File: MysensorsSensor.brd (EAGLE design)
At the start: 26.2 x 44.1 mm, 41 parts, among them IC1 TS5205, IC2 AT25DF512C-SSHN-B, IC3 ATSHA204A, Q1 FC-12M, U1 ATMEGA328P-AU

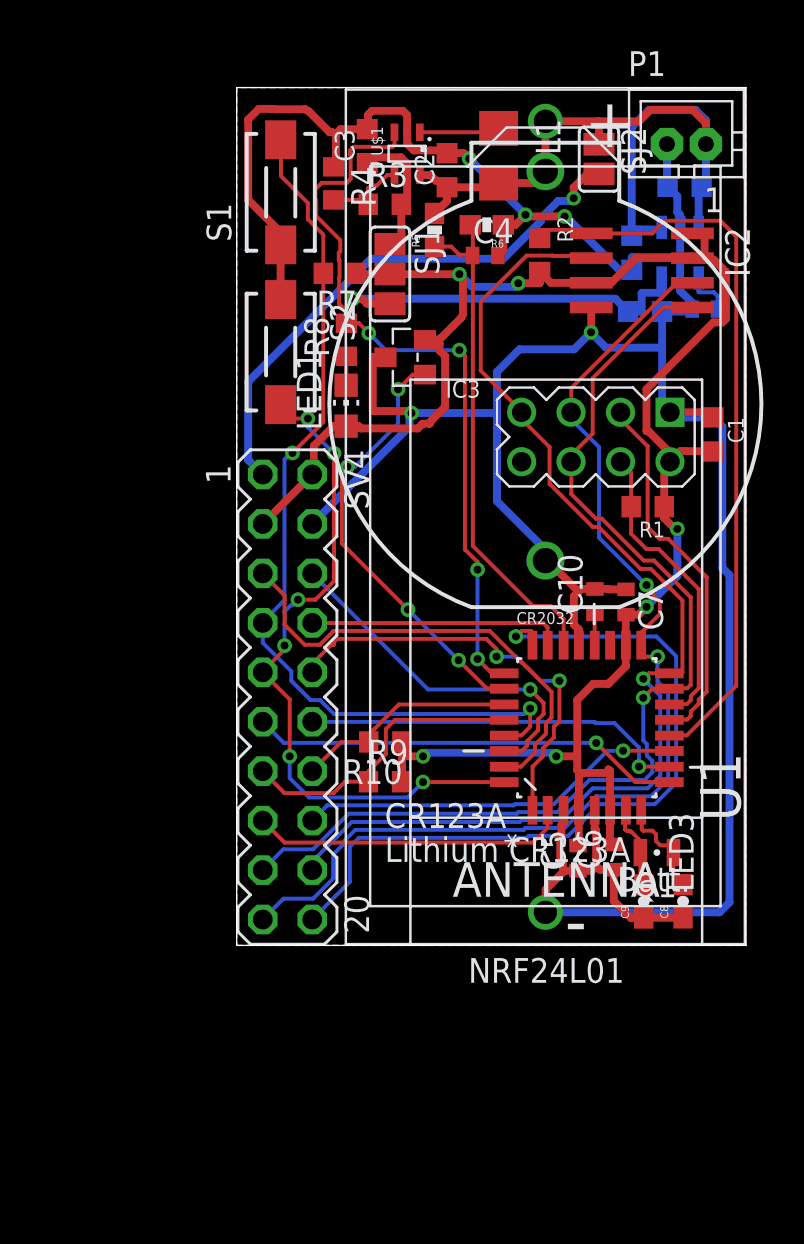
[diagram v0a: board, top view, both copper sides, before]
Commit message: 1. fix wrong boost converter footprint 2. connect led to A1 pin instead of A2 (which was used by the boost converter enable 3. change crystal footrint but not change the pcb
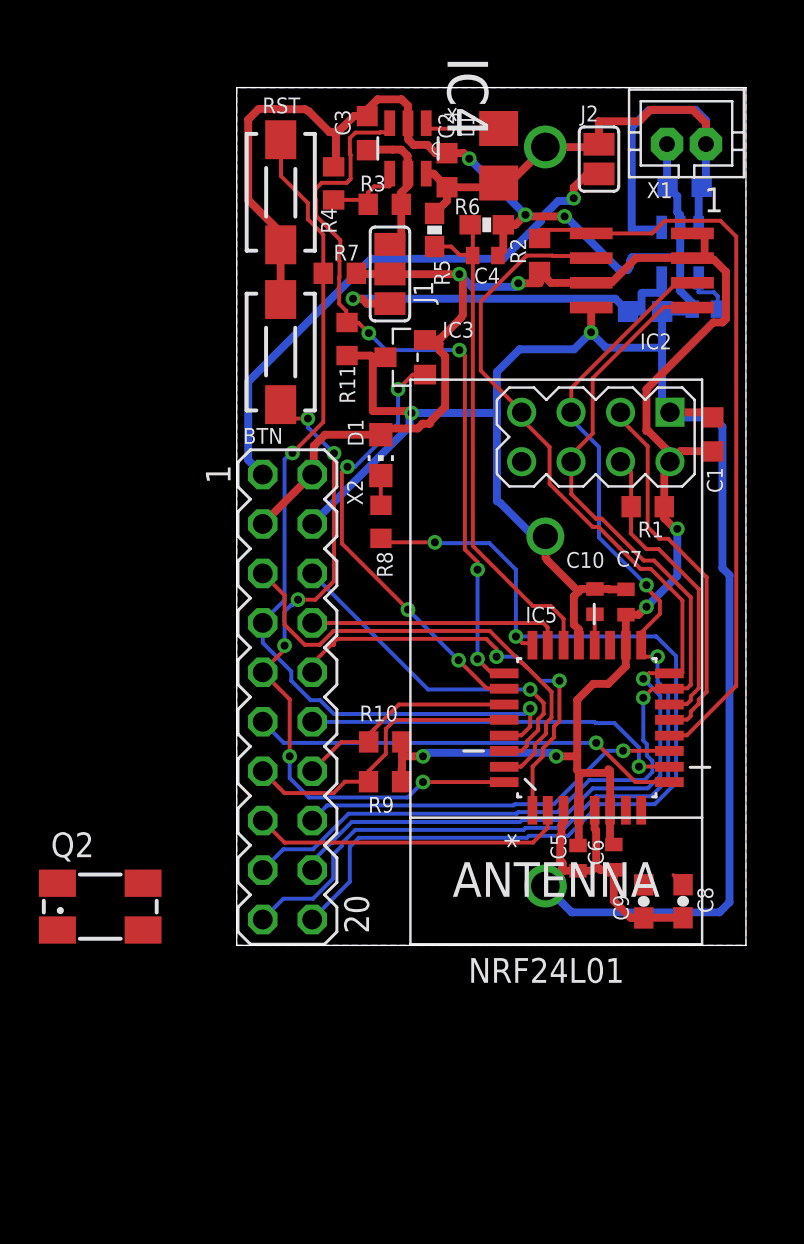
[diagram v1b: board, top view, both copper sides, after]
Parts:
- removed C11: 10u, rcl:C0603K
- removed LED1: (no value), led:CHIP-LED0805
- removed Q1: FC-12M, crystal:FC-12M
- removed U$1: MCP1640, pulseoxparts:SOT23-6
- added D1: (no value), led:CHIP-LED0805
- added IC4: MCP1640CT-I/CHY, Microchip_By_element14_Batch_1:SOT95P270X145-6N
- added Q2: (no value), crystal:CTS406
- added R11: 1M, resistor:R0603
- C10, C4, C5, C6, C7: value (none) -> 100n
- C12: value (none) -> 10n
- C8, C9: value 10u -> 22p
- CR123A: value (none) -> BAT_PACKCR123A; device Battery:TAKACHI_CR123A -> batteries:BH123A
- CR2032: value (none) -> 3V
- L1: value (none) -> 4.7u
- R1, R2, R3, R5, R7: value 100k -> 1M
- R10, R9: value 100k -> 10k
- R4: value 100k -> 620k
- R8: value 100k -> 1k
- moved R8 9.52 mm to (7.41, 21.8), turned to 270 degrees
- moved CR2032 1.24 mm to (15.9, 29.2), flipped to the bottom
- moved C3 0.67 mm to (6.71, 41.7)
- flipped CR123A to the bottom, turned to 90 degrees
- renumbered P1 to X1, S1 to RST, S2 to BTN, SJ1 to J1, SJ2 to J2, SV4 to X2, U1 to IC5
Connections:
- net A1: now also R8.2
- net A2: now also IC4.3, R11.1; no longer R8.2, U$1.P$3
- net GND: now also IC4.2, R11.2; no longer C11.2, U$1.P$2
- net N$1: now also IC4.4; no longer U$1.P$4
- net N$10: now also D1.C; no longer LED1.C
- net N$2: now also Q2.1; no longer Q1.1
- net N$4: now also IC4.1; no longer U$1.P$1
- net N$6: now also Q2.3; no longer Q1.2
- net VBAT: now also IC4.6; no longer C11.1, U$1.P$6
- net VBOOST: now also IC4.5; no longer U$1.P$5
- net VCC: now also D1.A; no longer LED1.A
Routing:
- net A1: track 39.9 -> 50.4 mm, vias 1 -> 2
- net N$2: track 5.31 -> 0.70 mm
- net N$6: track 4.37 -> 0.00 mm
- net VBAT: track 39.5 -> 36.9 mm
- net GND: track 163.2 -> 164.4 mm
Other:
- board text added: "MySensors 1.0"
- board text removed: "LED3"

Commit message: 1. rearrange nfr24l01 connector and atmega328p chip
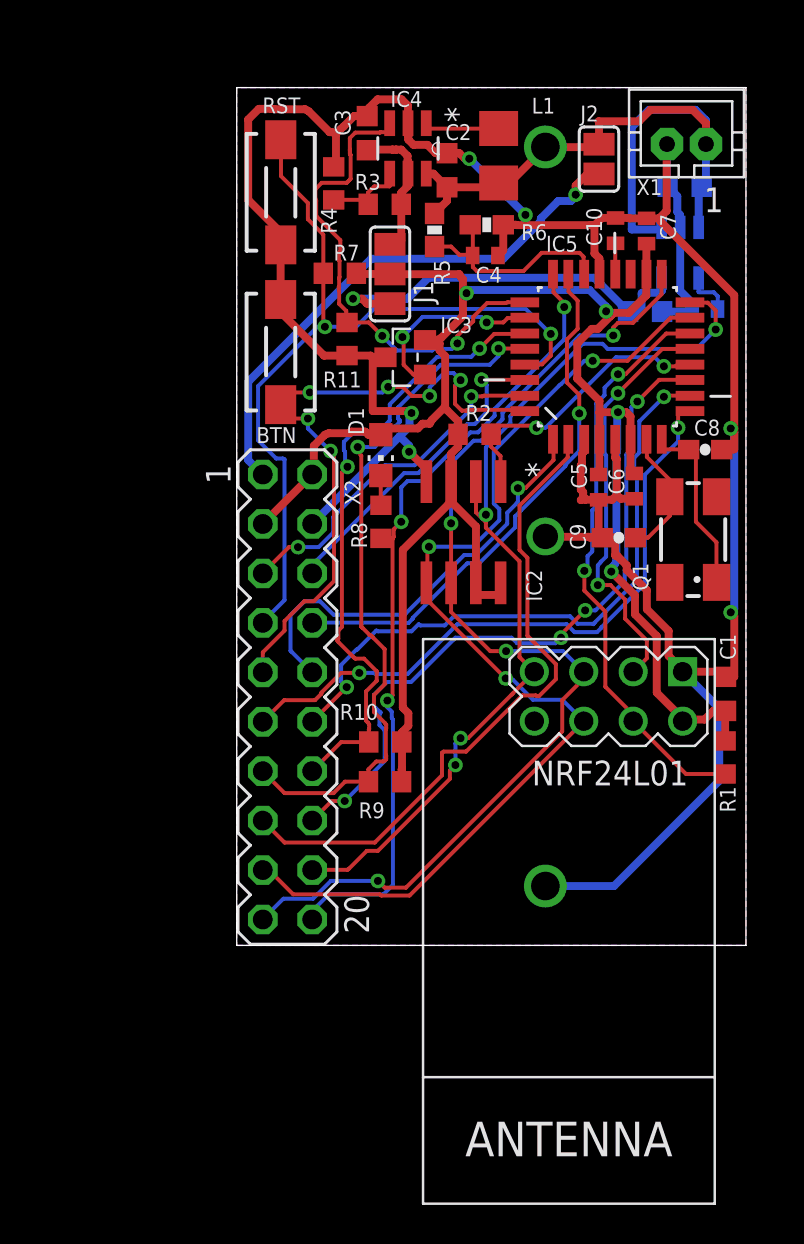
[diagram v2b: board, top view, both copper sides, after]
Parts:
- removed Q2: (no value), crystal:CTS406
- added Q1: (no value), crystal:CTS406
- moved C8 23.2 mm to (24.1, 25.5), turned to 180 degrees
- moved C10 19.1 mm to (19.5, 36.7)
- moved C5 19.1 mm to (18.6, 23.5)
- moved C7 19.1 mm to (21.1, 36.7)
- moved IC5 19.1 mm to (19.0, 30.2)
- moved C6 19.1 mm to (20.4, 23.6)
- moved C9 18.7 mm to (19.6, 20.9), turned to 0 degrees
- moved IC2 16.3 mm to (11.7, 21.2), turned to 180 degrees
- moved R1 13.5 mm to (25.1, 9.66), turned to 270 degrees
- moved C1 13.3 mm to (25.1, 12.9)
- moved NRF24L01 13.3 mm to (16.6, 1.36)
- moved R2 9.80 mm to (12.2, 26.3), turned to 180 degrees
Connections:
- net N$2: now also Q1.1; no longer Q2.1
- net N$6: now also Q1.3; no longer Q2.3
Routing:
- net D8: track 38.8 -> 15.1 mm, vias 0 -> 2
- net A4: track 11.5 -> 32.8 mm, vias 0 -> 2
- net A5: track 15.5 -> 36.6 mm, vias 0 -> 2
- net D4: track 16.3 -> 33.8 mm
- net D7: track 19.8 -> 37.0 mm, vias 1 -> 4
- net A7: track 26.4 -> 11.6 mm
- net A0: track 13.1 -> 27.6 mm, vias 0 -> 1
- net D10: track 15.6 -> 30.0 mm, vias 0 -> 2
- net A2: track 38.7 -> 25.5 mm, vias 4 -> 2
- net D6: track 19.9 -> 32.7 mm, vias 1 -> 2
- net A3: track 22.5 -> 9.69 mm, vias 4 -> 2
- net GND: track 164.4 -> 152.0 mm, vias 5 -> 6
- net D5: track 22.2 -> 33.2 mm, vias 1 -> 2
- net MISO: track 58.4 -> 48.5 mm, vias 1 -> 4
- net N$2: track 0.70 -> 9.54 mm
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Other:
- board text added: "MySensors 1.1"
- board text removed: "MySensors 1.0"

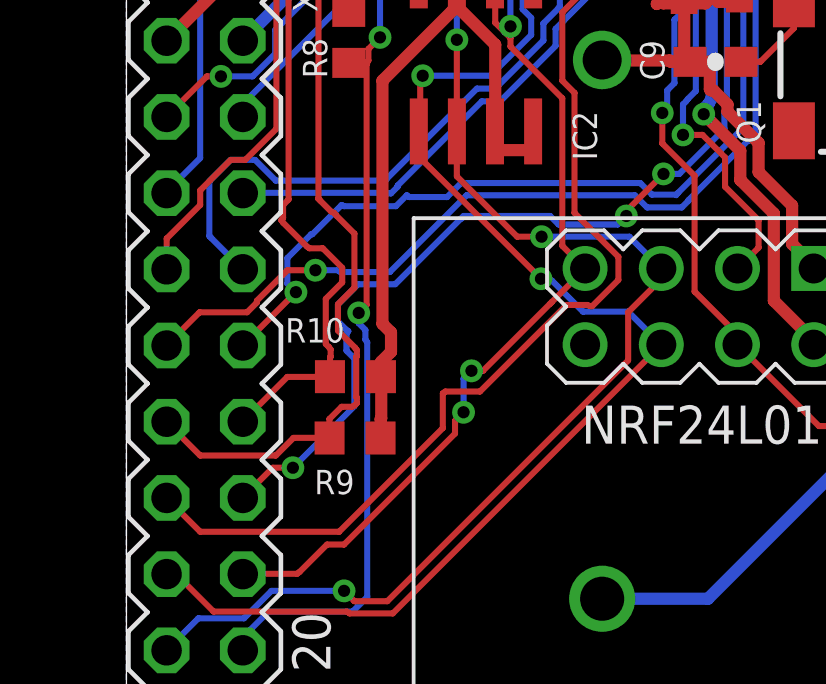
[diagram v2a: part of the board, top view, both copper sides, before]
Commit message: connect radio module irq with d2
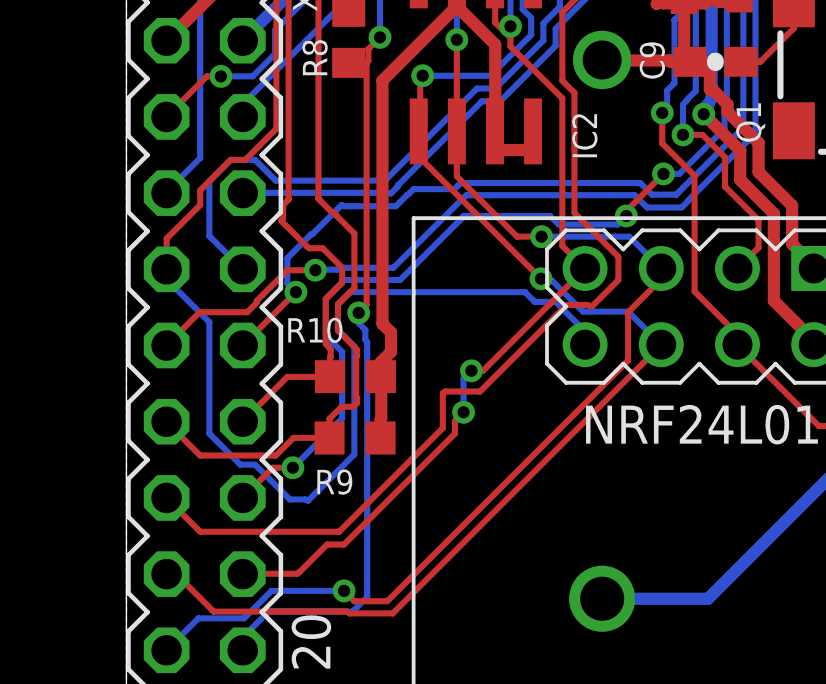
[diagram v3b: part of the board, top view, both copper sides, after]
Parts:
- IC1: value TS5205 -> APE8865Y5-30-HF-3
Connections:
- net D2: now also NRF24L01.8
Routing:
- net D2: track 33.6 -> 60.7 mm
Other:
- board text added: "MySensors 1.2"
- board text removed: "MySensors 1.1"
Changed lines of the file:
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@@
 <wire x1="26.162" y1="44.069" x2="0" y2="44.069" width="0" layer="20"/>
 <wire x1="0" y1="44.069" x2="0" y2="0" width="0" layer="20"/>
-<text x="1.524" y="26.924" size="1.4224" layer="22" font="vector" rot="MR90">MySensors 1.1</text>
+<text x="1.524" y="26.924" size="1.4224" layer="22" font="vector" rot="MR90">MySensors 1.2</text>
 </plain>
 <attributes>
@@
 <attribute name="VALUE" x="21.367396875" y="36.085440625" size="1.27" layer="27" rot="R90"/>
 </element>
-<element name="IC1" library="v-reg" package="SOT25" value="TS5205" x="22.7838" y="35.5854" smashed="yes" rot="MR180">
+<element name="IC1" library="v-reg" package="SOT25" value="APE8865Y5-30-HF-3" x="22.7838" y="35.5854" smashed="yes" rot="MR180">
 <attribute name="NAME" x="20.045684375" y="34.7370375" size="0.8128" layer="26" font="vector" rot="MR90"/>
 <attribute name="VALUE" x="20.8788" y="39.0144" size="1.27" layer="28" rot="MR180"/>
@@
 <wire x1="4.8768" y1="7.4168" x2="3.88111875" y2="6.421121875" width="0.2032" layer="1"/>
 <wire x1="5.547359375" y1="7.4168" x2="4.8768" y2="7.4168" width="0.2032" layer="1"/>
-<wire x1="7.59968125" y1="9.469121875" x2="5.547359375" y2="7.4168" width="0.2032" layer="16"/>
-<wire x1="7.59968125" y1="11.05408125" x2="7.59968125" y2="9.469121875" width="0.2032" layer="16"/>
-<wire x1="7.33551875" y1="11.318240625" x2="7.59968125" y2="11.05408125" width="0.2032" layer="16"/>
-<wire x1="7.33551875" y1="11.8872" x2="7.33551875" y2="11.318240625" width="0.2032" layer="16"/>
 <wire x1="20.0152" y1="25.217121875" x2="20.0152" y2="19.5072" width="0.2032" layer="16"/>
 <wire x1="3.88111875" y1="6.421121875" x2="3.878440625" y2="6.4104" width="0.2032" layer="1"/>
@@
 <wire x1="14.1224" y1="15.808959375" x2="14.40688125" y2="15.52448125" width="0.2032" layer="16"/>
 <wire x1="11.236959375" y1="15.808959375" x2="14.1224" y2="15.808959375" width="0.2032" layer="16"/>
-<wire x1="7.39648125" y1="11.96848125" x2="7.33551875" y2="11.8872" width="0.2032" layer="16"/>
 <via x="16.6624" y="15.808959375" extent="1-16" drill="0.4064"/>
 <wire x1="19.93391875" y1="18.714721875" x2="18.430240625" y2="17.211040625" width="0.2032" layer="16"/>
@@
 <via x="17.90191875" y="17.211040625" extent="1-16" drill="0.4064"/>
 <wire x1="11.15568125" y1="15.72768125" x2="11.176" y2="15.72768125" width="0.2032" layer="16"/>
-<wire x1="8.96111875" y1="13.533121875" x2="11.15568125" y2="15.72768125" width="0.2032" layer="16"/>
-<wire x1="7.7216" y1="13.533121875" x2="8.96111875" y2="13.533121875" width="0.2032" layer="16"/>
-<wire x1="7.051040625" y1="12.862559375" x2="7.7216" y2="13.533121875" width="0.2032" layer="16"/>
-<wire x1="7.051040625" y1="12.2936" x2="7.051040625" y2="12.862559375" width="0.2032" layer="16"/>
-<wire x1="7.3152" y1="12.029440625" x2="7.051040625" y2="12.2936" width="0.2032" layer="16"/>
 <wire x1="11.176" y1="15.72768125" x2="11.236959375" y2="15.808959375" width="0.2032" layer="16"/>
-<wire x1="7.3152" y1="12.029440625" x2="7.39648125" y2="11.96848125" width="0.2032" layer="16"/>
+<wire x1="7.19328125" y1="9.062721875" x2="5.547359375" y2="7.4168" width="0.2032" layer="16"/>
+<wire x1="7.19328125" y1="11.2776" x2="7.19328125" y2="9.062721875" width="0.2032" layer="16"/>
+<wire x1="6.644640625" y1="11.826240625" x2="7.19328125" y2="11.2776" width="0.2032" layer="16"/>
+<wire x1="6.644640625" y1="13.045440625" x2="6.644640625" y2="11.826240625" width="0.2032" layer="16"/>
+<wire x1="7.274559375" y1="13.675359375" x2="6.644640625" y2="13.045440625" width="0.2032" layer="16"/>
+<wire x1="9.12368125" y1="13.675359375" x2="7.274559375" y2="13.675359375" width="0.2032" layer="16"/>
+<wire x1="11.09471875" y1="15.6464" x2="9.12368125" y2="13.675359375" width="0.2032" layer="16"/>
+<wire x1="11.09471875" y1="15.6464" x2="11.15568125" y2="15.72768125" width="0.2032" layer="16"/>
 </signal>
 <signal name="D2">
@@
 <via x="3.6576" y="27.066240625" extent="1-16" drill="0.4064"/>
 <via x="4.815840625" y="25.4" extent="1-16" drill="0.4064"/>
+<contactref element="NRF24L01" pad="8"/>
+<wire x1="7.59968125" y1="7.863840625" x2="6.055359375" y2="6.319521875" width="0.2032" layer="16"/>
+<wire x1="7.59968125" y1="11.46048125" x2="7.59968125" y2="7.863840625" width="0.2032" layer="16"/>
+<wire x1="7.051040625" y1="12.009121875" x2="7.59968125" y2="11.46048125" width="0.2032" layer="16"/>
+<wire x1="7.051040625" y1="12.862559375" x2="7.051040625" y2="12.009121875" width="0.2032" layer="16"/>
+<wire x1="7.457440625" y1="13.268959375" x2="7.051040625" y2="12.862559375" width="0.2032" layer="16"/>
+<wire x1="13.28928125" y1="13.268959375" x2="7.457440625" y2="13.268959375" width="0.2032" layer="16"/>
+<wire x1="13.6144" y1="12.943840625" x2="13.28928125" y2="13.268959375" width="0.2032" layer="16"/>
+<wire x1="14.30528125" y1="12.943840625" x2="13.6144" y2="12.943840625" width="0.2032" layer="16"/>
+<wire x1="15.280640625" y1="11.96848125" x2="14.30528125" y2="12.943840625" width="0.2032" layer="16"/>
+<wire x1="15.280640625" y1="11.521440625" x2="15.280640625" y2="11.96848125" width="0.2032" layer="16"/>
+<wire x1="15.280640625" y1="11.521440625" x2="15.2888625" y2="11.51888125" width="0.2032" layer="16"/>
+<wire x1="1.34111875" y1="13.69568125" x2="1.34111875" y2="14.0208" width="0.2032" layer="16"/>
+<wire x1="2.76351875" y1="12.27328125" x2="1.34111875" y2="13.69568125" width="0.2032" layer="16"/>
+<wire x1="2.76351875" y1="8.554721875" x2="2.76351875" y2="12.27328125" width="0.2032" layer="16"/>
+<wire x1="3.799840625" y1="7.5184" x2="2.76351875" y2="8.554721875" width="0.2032" layer="16"/>
+<wire x1="4.28751875" y1="7.5184" x2="3.799840625" y2="7.5184" width="0.2032" layer="16"/>
+<wire x1="5.445759375" y1="6.360159375" x2="4.28751875" y2="7.5184" width="0.2032" layer="16"/>
+<wire x1="5.953759375" y1="6.360159375" x2="5.445759375" y2="6.360159375" width="0.2032" layer="16"/>
+<wire x1="1.34111875" y1="14.0208" x2="1.338440625" y2="14.0304" width="0.2032" layer="16"/>
+<wire x1="5.953759375" y1="6.360159375" x2="6.055359375" y2="6.319521875" width="0.2032" layer="16"/>
 </signal>
 <signal name="D3">
@@
 <wire x1="17.129759375" y1="16.906240625" x2="17.515840625" y2="16.520159375" width="0.2032" layer="16"/>
 <wire x1="11.15568125" y1="16.906240625" x2="17.129759375" y2="16.906240625" width="0.2032" layer="16"/>
-<wire x1="10.68831875" y1="16.43888125" x2="11.15568125" y2="16.906240625" width="0.2032" layer="16"/>
-<wire x1="9.42848125" y1="16.43888125" x2="10.68831875" y2="16.43888125" width="0.2032" layer="16"/>
 <wire x1="18.328640625" y1="16.520159375" x2="18.328640625" y2="16.499840625" width="0.2032" layer="16"/>
-<wire x1="9.42848125" y1="16.43888125" x2="9.3472" y2="16.499840625" width="0.2032" layer="16"/>
 <wire x1="18.3896" y1="16.581121875" x2="20.482559375" y2="18.67408125" width="0.2032" layer="16"/>
 <wire x1="20.482559375" y1="18.67408125" x2="20.563840625" y2="18.735040625" width="0.2032" layer="16"/>
 <wire x1="18.3896" y1="16.581121875" x2="18.328640625" y2="16.520159375" width="0.2032" layer="16"/>
+<wire x1="10.932159375" y1="16.703040625" x2="11.0744" y2="16.84528125" width="0.2032" layer="16"/>
+<wire x1="9.57071875" y1="16.703040625" x2="10.932159375" y2="16.703040625" width="0.2032" layer="16"/>
+<wire x1="9.42848125" y1="16.5608" x2="9.57071875" y2="16.703040625" width="0.2032" layer="16"/>
+<wire x1="11.0744" y1="16.84528125" x2="11.15568125" y2="16.906240625" width="0.2032" layer="16"/>
+<wire x1="9.42848125" y1="16.5608" x2="9.3472" y2="16.499840625" width="0.2032" layer="16"/>
 </signal>
 <signal name="D5">
 <contactref element="X2" pad="11"/>
 <contactref element="IC5" pad="9"/>
-<wire x1="6.2992" y1="14.00048125" x2="7.051040625" y2="14.00048125" width="0.2032" layer="16"/>
 <wire x1="5.36448125" y1="14.00048125" x2="6.2992" y2="14.00048125" width="0.2032" layer="1"/>
 <wire x1="4.34848125" y1="12.98448125" x2="5.36448125" y2="14.00048125" width="0.2032" layer="1"/>
@@
 <via x="6.2992" y="14.00048125" extent="1-16" drill="0.4064"/>
 <wire x1="11.338559375" y1="16.499840625" x2="16.94688125" y2="16.499840625" width="0.2032" layer="16"/>
-<wire x1="8.778240625" y1="13.939521875" x2="11.338559375" y2="16.499840625" width="0.2032" layer="16"/>
-<wire x1="7.13231875" y1="13.939521875" x2="8.778240625" y2="13.939521875" width="0.2032" layer="16"/>
-<wire x1="7.13231875" y1="13.939521875" x2="7.051040625" y2="14.00048125" width="0.2032" layer="16"/>
 <wire x1="20.970240625" y1="24.1808" x2="20.970240625" y2="18.552159375" width="0.2032" layer="16"/>
 <wire x1="22.67711875" y1="25.88768125" x2="20.970240625" y2="24.1808" width="0.2032" layer="16"/>
@@
 <wire x1="16.94688125" y1="16.499840625" x2="17.35328125" y2="16.093440625" width="0.2032" layer="16"/>
 <wire x1="20.90928125" y1="18.47088125" x2="20.970240625" y2="18.552159375" width="0.2032" layer="16"/>
+<wire x1="7.03071875" y1="14.0208" x2="6.31951875" y2="14.0208" width="0.2032" layer="16"/>
+<wire x1="7.09168125" y1="14.081759375" x2="7.03071875" y2="14.0208" width="0.2032" layer="16"/>
+<wire x1="8.900159375" y1="14.081759375" x2="7.09168125" y2="14.081759375" width="0.2032" layer="16"/>
+<wire x1="11.25728125" y1="16.43888125" x2="8.900159375" y2="14.081759375" width="0.2032" layer="16"/>
+<wire x1="6.31951875" y1="14.0208" x2="6.2992" y2="14.00048125" width="0.2032" layer="16"/>
+<wire x1="11.25728125" y1="16.43888125" x2="11.338559375" y2="16.499840625" width="0.2032" layer="16"/>
 </signal>
 <signal name="A3">
